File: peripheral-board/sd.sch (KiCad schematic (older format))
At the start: 9 parts, among them CON8001 SD_Card, Q8001 BSS84LT1G

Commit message: routed traces.
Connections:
- net RESET: now reaches CON8001.9 (DAT2)
- no-connect marks 2 -> 1
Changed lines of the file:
@@
 	2250 3450 3950 3450
 NoConn ~ 3950 2950
-NoConn ~ 3950 3750
 $Comp
 L C_Small C8004
@@
 	3950 3650 3200 3650
 $Comp
-L +3V3 #PWR081
+L +3V3 #PWR085
 U 1 1 582229DC
 P 2500 2400
-F 0 "#PWR081" H 2500 2250 50  0001 C CNN
+F 0 "#PWR085" H 2500 2250 50  0001 C CNN
 F 1 "+3V3" H 2515 2573 50  0000 C CNN
 F 2 "" H 2500 2400 50  0000 C CNN
@@
 $EndComp
 $Comp
-L GND #PWR082
+L GND #PWR086
 U 1 1 582229F6
 P 2800 2750
-F 0 "#PWR082" H 2800 2500 50  0001 C CNN
+F 0 "#PWR086" H 2800 2500 50  0001 C CNN
 F 1 "GND" V 2805 2622 50  0000 R CNN
 F 2 "" H 2800 2750 50  0000 C CNN
@@
 $EndComp
 $Comp
-L GND #PWR083
+L GND #PWR087
 U 1 1 58222A19
 P 2200 2750
-F 0 "#PWR083" H 2200 2500 50  0001 C CNN
+F 0 "#PWR087" H 2200 2500 50  0001 C CNN
 F 1 "GND" V 2205 2622 50  0000 R CNN
 F 2 "" H 2200 2750 50  0000 C CNN
@@
 $EndComp
 $Comp
-L GND #PWR084
+L GND #PWR088
 U 1 1 58222AC6
 P 4800 2100
-F 0 "#PWR084" H 4800 1850 50  0001 C CNN
+F 0 "#PWR088" H 4800 1850 50  0001 C CNN
 F 1 "GND" H 4805 1927 50  0000 C CNN
 F 2 "" H 4800 2100 50  0000 C CNN
@@
 $EndComp
 $Comp
-L +3V3 #PWR085
+L +3V3 #PWR089
 U 1 1 58222AE2
 P 4800 1700
-F 0 "#PWR085" H 4800 1550 50  0001 C CNN
+F 0 "#PWR089" H 4800 1550 50  0001 C CNN
 F 1 "+3V3" H 4815 1873 50  0000 C CNN
 F 2 "" H 4800 1700 50  0000 C CNN
@@
 	4800 2050 4800 2100
 $Comp
-L GND #PWR086
+L GND #PWR090
 U 1 1 58222B2D
 P 5850 3200
-F 0 "#PWR086" H 5850 2950 50  0001 C CNN
+F 0 "#PWR090" H 5850 2950 50  0001 C CNN
 F 1 "GND" V 5855 3072 50  0000 R CNN
 F 2 "" H 5850 3200 50  0000 C CNN
@@
 Connection ~ 6450 3450
 $Comp
-L +3V3 #PWR087
+L +3V3 #PWR091
 U 1 1 582235F2
 P 6600 2800
-F 0 "#PWR087" H 6600 2650 50  0001 C CNN
+F 0 "#PWR091" H 6600 2650 50  0001 C CNN
 F 1 "+3V3" H 6615 2973 50  0000 C CNN
 F 2 "" H 6600 2800 50  0000 C CNN
@@
 $EndComp
 $Comp
-L GND #PWR088
+L GND #PWR092
 U 1 1 58A4EBF7
 P 3700 5200
-F 0 "#PWR088" H 1950 200 50  0001 C CNN
+F 0 "#PWR092" H 1950 200 50  0001 C CNN
 F 1 "GND" H 3705 5027 50  0000 C CNN
 F 2 "" H 1950 450 50  0001 C CNN
@@
 $EndComp
 $Comp
-L +3V3 #PWR089
+L +3V3 #PWR093
 U 1 1 58A4ED0D
 P 3700 4200
-F 0 "#PWR089" H 1650 100 50  0001 C CNN
+F 0 "#PWR093" H 1650 100 50  0001 C CNN
 F 1 "+3V3" H 3715 4373 50  0000 C CNN
 F 2 "" H 1650 250 50  0001 C CNN
@@
 	3250 4400 3400 4400
 Connection ~ 3250 3650
+Text GLabel 3950 3750 0    60   Output ~ 0
+RESET
 $EndSCHEMATC

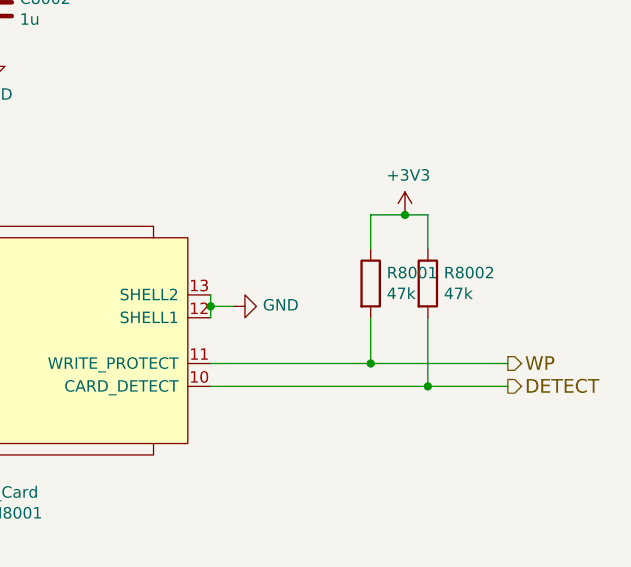
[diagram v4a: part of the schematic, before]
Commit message: fixed various drc errors
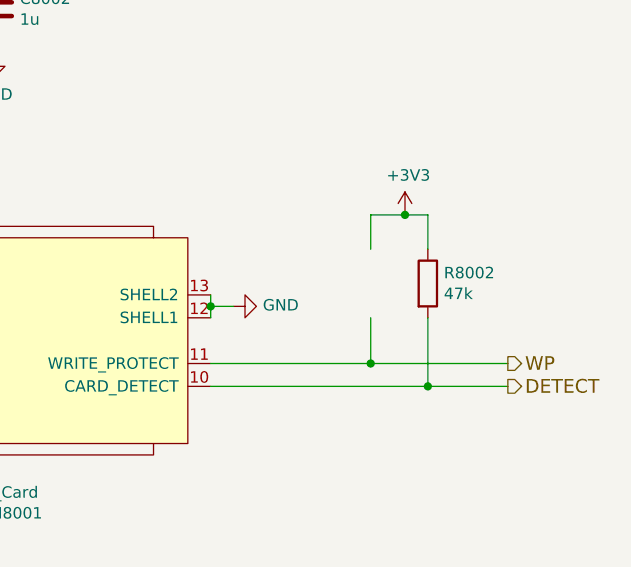
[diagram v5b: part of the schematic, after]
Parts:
- removed R8001: 47k, Resistors_SMD:R_0805, symbol R
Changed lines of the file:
@@
 	5750 3550 7050 3550
-$Comp
-L R R8001
-U 1 1 582234E6
-P 6450 3100
-F 0 "R8001" H 6520 3146 50  0000 L CNN
-F 1 "47k" H 6520 3055 50  0000 L CNN
-F 2 "Resistors_SMD:R_0805" V 6380 3100 50  0001 C CNN
-F 3 "" H 6450 3100 50  0000 C CNN
-	1    6450 3100
-	1    0    0    -1
-$EndComp
 $Comp
 L R R8002

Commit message: minor fixes
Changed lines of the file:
@@
 Wire Wire Line
 	2250 3450 3950 3450
-NoConn ~ 3950 2950
+NoConn ~ 3950 3750
 $Comp
 L C_Small C8004
@@
 	3950 3650 3200 3650
 $Comp
-L +3V3 #PWR087
+L +3V3 #PWR088
 U 1 1 582229DC
 P 2500 2400
-F 0 "#PWR087" H 2500 2250 50  0001 C CNN
+F 0 "#PWR088" H 2500 2250 50  0001 C CNN
 F 1 "+3V3" H 2515 2573 50  0000 C CNN
 F 2 "" H 2500 2400 50  0000 C CNN
@@
 $EndComp
 $Comp
-L GND #PWR088
+L GND #PWR089
 U 1 1 582229F6
 P 2800 2750
-F 0 "#PWR088" H 2800 2500 50  0001 C CNN
+F 0 "#PWR089" H 2800 2500 50  0001 C CNN
 F 1 "GND" V 2805 2622 50  0000 R CNN
 F 2 "" H 2800 2750 50  0000 C CNN
@@
 $EndComp
 $Comp
-L GND #PWR089
+L GND #PWR090
 U 1 1 58222A19
 P 2200 2750
-F 0 "#PWR089" H 2200 2500 50  0001 C CNN
+F 0 "#PWR090" H 2200 2500 50  0001 C CNN
 F 1 "GND" V 2205 2622 50  0000 R CNN
 F 2 "" H 2200 2750 50  0000 C CNN
@@
 $EndComp
 $Comp
-L GND #PWR090
+L GND #PWR091
 U 1 1 58222AC6
 P 4800 2100
-F 0 "#PWR090" H 4800 1850 50  0001 C CNN
+F 0 "#PWR091" H 4800 1850 50  0001 C CNN
 F 1 "GND" H 4805 1927 50  0000 C CNN
 F 2 "" H 4800 2100 50  0000 C CNN
@@
 $EndComp
 $Comp
-L +3V3 #PWR091
+L +3V3 #PWR092
 U 1 1 58222AE2
 P 4800 1700
-F 0 "#PWR091" H 4800 1550 50  0001 C CNN
+F 0 "#PWR092" H 4800 1550 50  0001 C CNN
 F 1 "+3V3" H 4815 1873 50  0000 C CNN
 F 2 "" H 4800 1700 50  0000 C CNN
@@
 	4800 2050 4800 2100
 $Comp
-L GND #PWR092
+L GND #PWR093
 U 1 1 58222B2D
 P 5850 3200
-F 0 "#PWR092" H 5850 2950 50  0001 C CNN
+F 0 "#PWR093" H 5850 2950 50  0001 C CNN
 F 1 "GND" V 5855 3072 50  0000 R CNN
 F 2 "" H 5850 3200 50  0000 C CNN
@@
 Connection ~ 6450 3450
 $Comp
-L +3V3 #PWR093
+L +3V3 #PWR094
 U 1 1 582235F2
 P 6600 2800
-F 0 "#PWR093" H 6600 2650 50  0001 C CNN
+F 0 "#PWR094" H 6600 2650 50  0001 C CNN
 F 1 "+3V3" H 6615 2973 50  0000 C CNN
 F 2 "" H 6600 2800 50  0000 C CNN
@@
 $EndComp
 $Comp
-L GND #PWR094
+L GND #PWR095
 U 1 1 58A4EBF7
 P 3700 5200
-F 0 "#PWR094" H 1950 200 50  0001 C CNN
+F 0 "#PWR095" H 1950 200 50  0001 C CNN
 F 1 "GND" H 3705 5027 50  0000 C CNN
 F 2 "" H 1950 450 50  0001 C CNN
@@
 $EndComp
 $Comp
-L +3V3 #PWR095
+L +3V3 #PWR096
 U 1 1 58A4ED0D
 P 3700 4200
-F 0 "#PWR095" H 1650 100 50  0001 C CNN
+F 0 "#PWR096" H 1650 100 50  0001 C CNN
 F 1 "+3V3" H 3715 4373 50  0000 C CNN
 F 2 "" H 1650 250 50  0001 C CNN
@@
 	3250 4400 3400 4400
 Connection ~ 3250 3650
-Text GLabel 3950 3750 0    60   Output ~ 0
+Text GLabel 3950 2950 0    60   Output ~ 0
 RESET
 $EndSCHEMATC
